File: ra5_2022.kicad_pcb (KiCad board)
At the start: 2 copper layers, 158 parts, among them CN1 KF250-3.5-2P-2, CN2 MX15EDGRHC-3.5-2*02P-BK01-CU-A, CN3 KF250-3.5-2P-2, CN4 KF250-3.5-2P-2, J1 Bus_M.2_Socket_E, J2 Conn_01x04_Socket, J3 MX15EDGRHC-3.5-2x03P, Q1 BC817, Q2 BC817, Q3 BC817, Q4 BC817, Q5 BC817, U1 STM8S003F3P, U10 ATM90E32AS-AU-R, U11 K3-2268P, U12 ADS1115IDGS, U2 TPS54202DDC, U3 B0303S-1WR2, U4 JTD6206-3.3V, U5 ISO7741N1-Y, U6 CS817X20LS, U7 AMS1117-3.3, U8 DB126V-5.0-2P-BK-P, U9 DB126V-5.0-2P-BK-P, Y1 ABM8G-16.384MHZ-18-D2Y-T

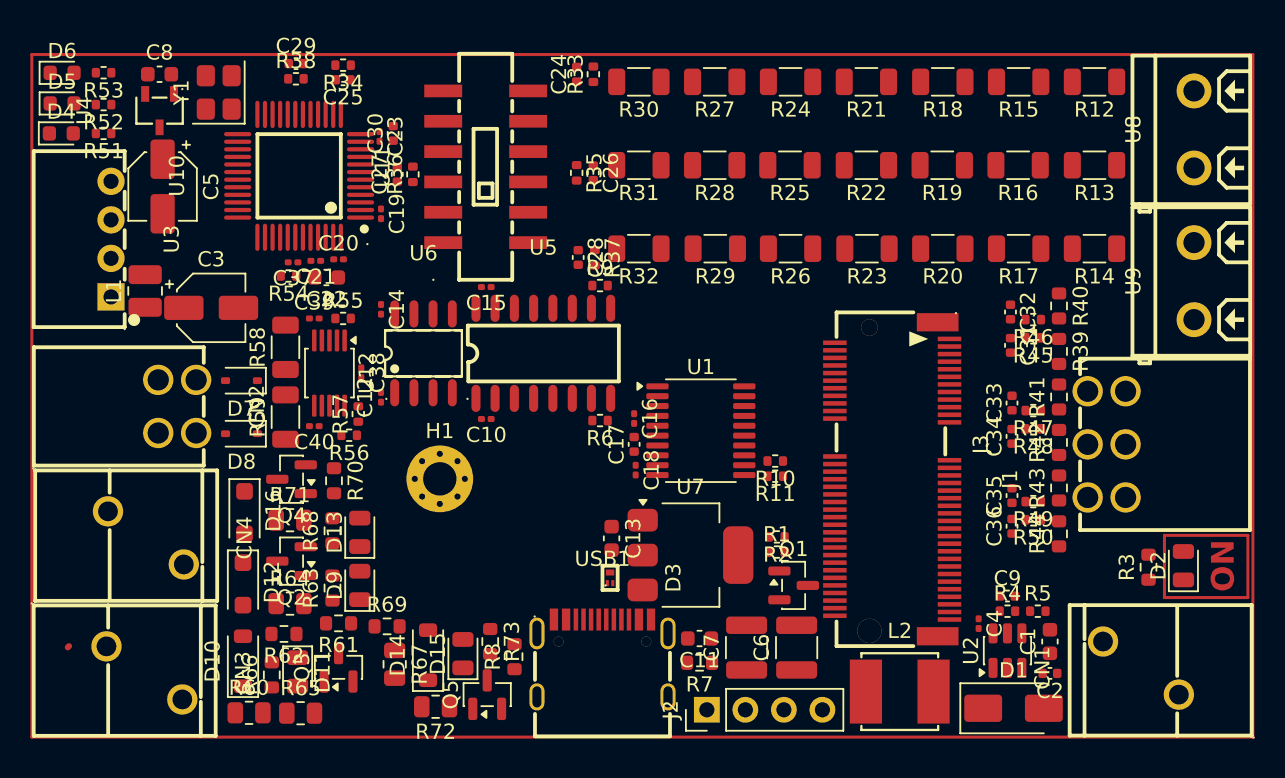
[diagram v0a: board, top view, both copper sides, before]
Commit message: Fix USB_90R/HighSpeed netclass clearance for M.2 socket pitch, route USB diff pair, add board render doc
Netclass clearance (0.25mm) exceeded the J1 M.2 socket's actual 0.5mm-pitch
pad spacing (~0.2mm) and the USB_90R diff pair gap (0.1mm), blocking the
interactive router from escaping J1's pads. Lowered USB_90R and HighSpeed
clearance to 0.2mm and the board's global min_clearance/min_connection to
match, plus a custom rule permitting the 0.1mm DP/DN internal gap. Routed
the USB_DP/USB_DN differential pair from J1 to D3.

Added view/ with finished-board renders and a short board description.
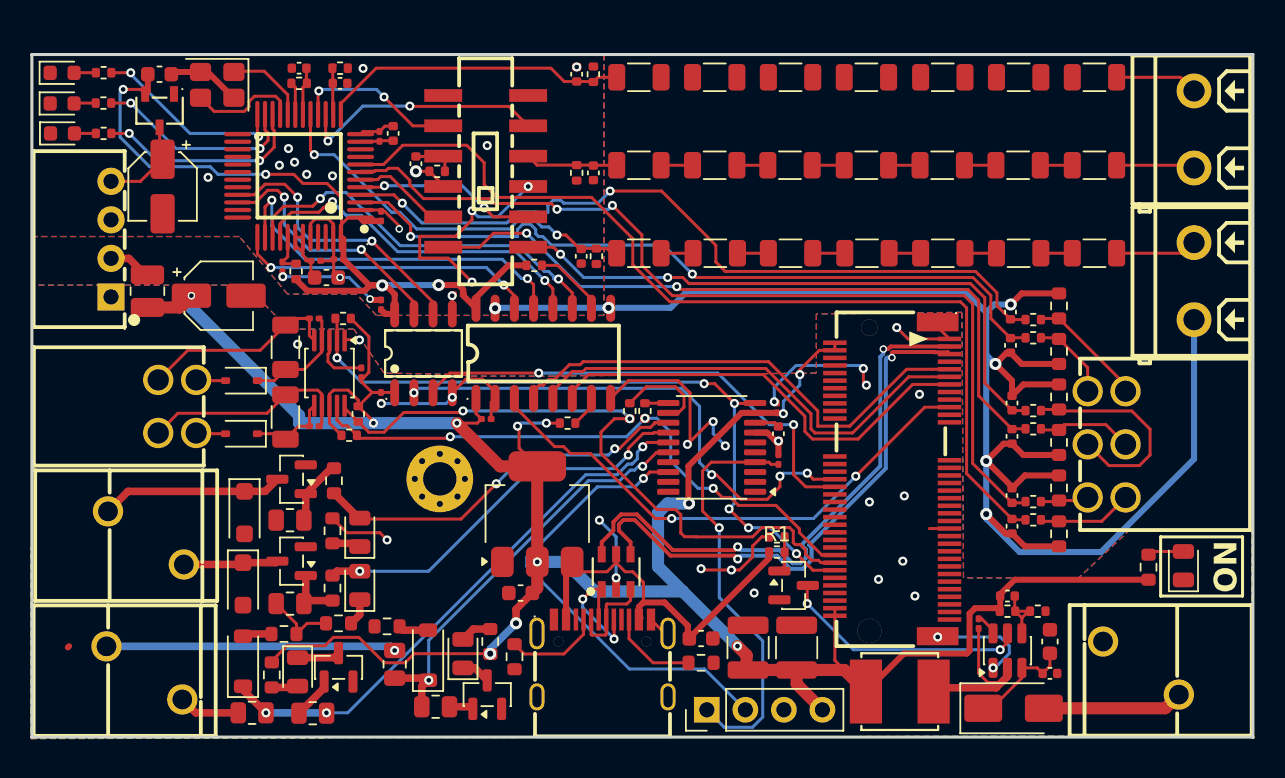
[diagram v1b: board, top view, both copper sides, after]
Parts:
- added REF**: ESD-Logo_8.9x8mm_SilkScreen, Symbol:ESD-Logo_8.9x8mm_SilkScreen, B.Cu at (167.2, 79.6)
- added REF**: WEEE-Logo_5.6x8mm_SilkScreen, Symbol:WEEE-Logo_5.6x8mm_SilkScreen, B.Cu at (158.8, 79.6)
- D3: value PESD5V0L2UM,315 -> USBLC6-2SC6; footprint ra5_2022:SOT-883-3_L1.0-W0.6-BR -> ra5_2022:SOT-23-6_L2.9-W1.6-P0.95-LS2.8-BL
- moved U7 10.5 mm to (141.8, 104.0), turned to 90 degrees
- moved C18 10.2 mm to (157.6, 97.0), turned to 90 degrees
- moved R10 10.1 mm to (147.9, 97.2), turned to 90 degrees
- moved C16 9.89 mm to (157.7, 100.4), turned to 90 degrees
- moved R11 9.60 mm to (148.9, 97.2), turned to 90 degrees
- moved C17 9.54 mm to (157.7, 98.7), turned to -90 degrees
- moved C13 7.00 mm to (140.7, 109.2), turned to 0 degrees
- moved R9 4.54 mm to (141.6, 87.6), turned to 180 degrees
- moved R6 2.15 mm to (143.8, 98.0), turned to 0 degrees
- moved C15 1.90 mm to (136.6, 89.5), turned to 0 degrees
- moved R36 1.61 mm to (135.2, 81.4), turned to 0 degrees
- moved C27 1.41 mm to (133.8, 80.9)
- moved U1 1.31 mm to (153.3, 99.6), turned to 180 degrees
- moved C3 0.94 mm to (120.8, 89.6)
- moved R65 0.80 mm to (127.0, 117.1)
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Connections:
- D3 pad 1: /MCU/USB_DN -> /MCU/USB_D+
- D3 pad 2: /MCU/USB_DP -> GND
- D3 pad 3: GND -> /MCU/USB_D-
- U1 pad 13: /MCU/Digital IO/DIN1_MCU -> /MCU/Digital IO/DO2_MCU
- U1 pad 14: /MCU/Digital IO/DIN2_MCU -> /MCU/Digital IO/DO1_MCU
- U1 pad 15: /MCU/Digital IO/DO1_MCU -> /MCU/Digital IO/DIN1_MCU
- U1 pad 16: /MCU/Digital IO/DO2_MCU -> /MCU/Digital IO/DIN2_MCU
- USB1 pad A6: /MCU/USB_DP -> /MCU/USB_D+
- USB1 pad A7: /MCU/USB_DN -> /MCU/USB_D-
- USB1 pad B6: /MCU/USB_DP -> /MCU/USB_D+
- USB1 pad B7: /MCU/USB_DN -> /MCU/USB_D-
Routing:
- net VDD: track 0.00 -> 169.1 mm, vias 0 -> 12
- net GND2: track 0.00 -> 153.7 mm, vias 0 -> 24
- net GND: track 0.12 -> 75.8 mm, vias 0 -> 26
- net /MCU/M90E32AS/I3N: track 0.00 -> 62.8 mm
- net /MCU/M90E32AS/I3P: track 0.00 -> 60.8 mm, vias 0 -> 2
- net VDD2: track 0.00 -> 55.0 mm, vias 0 -> 4
- net /MCU/M90E32AS/I1N: track 0.00 -> 50.6 mm, vias 0 -> 2
- net /MCU/M90E32AS/I1P: track 0.00 -> 50.0 mm, vias 0 -> 2
- net /MCU/M90E32AS/I2N_SW: track 0.00 -> 47.8 mm, vias 0 -> 2
- net /MCU/ALERT: track 0.00 -> 47.2 mm, vias 0 -> 6
- net /MCU/SCL: track 0.00 -> 44.4 mm, vias 0 -> 2
- net /MCU/M90E32AS/I2P_SW: track 0.00 -> 40.5 mm, vias 0 -> 2
- net /MCU/SDA: track 0.00 -> 39.8 mm, vias 0 -> 3
- net /MCU/USB_DP: track 0.00 -> 37.6 mm, vias 0 -> 2
- net /MCU/USB_DN: track 0.00 -> 36.9 mm, vias 0 -> 2
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- added copper zone on B.Cu, net GND
- added copper zone on F.Cu, net GND
- added copper zone on B.Cu, net GND2
- added copper zone on F.Cu, net GND2
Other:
- board outline added: 80.5 x 45 mm
- board text added: "+"
- board text added: "-"
- board text added: "AIN1"
- board text added: "AIN2"
- board text added: "DIN1"
- board text added: "DIN2"
- board text added: "DOUT1"
- board text added: "DOUT2"
- board text added: "GND"
- board text added: "VCC"
